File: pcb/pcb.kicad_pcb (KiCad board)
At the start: 2 copper layers, 299.5 x 113.5 mm, 228 parts, among them SW1 SW_DIP_x01_XKB_TS_2030, SW2 SW_DIP_x01_XKB_TS_2030, U1 RP2040, U2 Memory_Flash_W25Q64_XSON, U3 NCP114ASN330T1G, X1 12.000MHz

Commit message: R  pickle.py -> dumploc.py M  notes/spi M  pcb/pcb.kicad_pcb M  pcb/pcb.kicad_prl M  pcb/pcb.kicad_pro M  pcb/pcb.kicad_sch M  placefp.py M  tmr-footprints/LED-6028.kicad_mod
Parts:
- added R14: 33R, tmr-lib:R_0603_1608Metric, B.Cu at (26.9, 57.8)
- added R17: 33R, tmr-lib:R_0603_1608Metric, F.Cu at (21.4, 90.5)
- added R18: 33R, tmr-lib:R_0603_1608Metric, F.Cu at (21.4, 93.0)
- added R19: 33R, tmr-lib:R_0603_1608Metric, F.Cu at (21.4, 95.5)
- added R20: 33R, tmr-lib:R_0603_1608Metric, F.Cu at (21.4, 98.0)
- added R21: 33R, tmr-lib:R_0603_1608Metric, F.Cu at (25.4, 88.0)
- added R22: 33R, tmr-lib:R_0603_1608Metric, F.Cu at (25.4, 90.5)
- added R23: 33R, tmr-lib:R_0603_1608Metric, F.Cu at (25.4, 93.0)
- added R24: 33R, tmr-lib:R_0603_1608Metric, F.Cu at (25.4, 95.5)
- added R25: 33R, tmr-lib:R_0603_1608Metric, F.Cu at (25.4, 98.0)
- added R9: 33R, tmr-lib:R_0603_1608Metric, B.Cu at (24.9, 56.0)
- R1, R2, R3: moved to F.Cu
- moved C24 110.5 mm to (154.4, 48.0), turned to 180 degrees
- moved C22 64.6 mm to (26.6, 36.9), turned to -90 degrees
- moved ADC2 19.1 mm to (151.9, 23.9)
- moved ADC7 19.1 mm to (171.0, 23.8)
- moved C14 18.9 mm to (4.62, 49.1)
- moved ADC1 18.4 mm to (151.1, 12.4)
- moved C13 15.4 mm to (7.89, 49.2), turned to 180 degrees
- moved H4 13.3 mm to (12.3, 12.3)
- moved C19 9.56 mm to (23.2, 67.6)
- moved C9 9.04 mm to (11.2, 62.6)
- moved C23 7.58 mm to (54.9, 52.0), turned to -90 degrees
- moved C8 5.68 mm to (11.2, 64.1)
- moved C21 4.05 mm to (98.0, 34.6)
- moved C1 3.72 mm to (12.2, 51.5), turned to -90 degrees
- moved U2 3.55 mm to (17.7, 53.5)
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- renumbered LedDr1 to LD1, USBCon1 to USB1
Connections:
- ADC1 pad 10: unconnected-(ADC1-~{CS}/SHDN-Pad10) -> /GPIO2
- ADC2 pad 1: ANA_16 -> ANA_23
- ADC2 pad 10: unconnected-(ADC2-~{CS}/SHDN-Pad10) -> /GPIO3
- ADC2 pad 2: ANA_17 -> ANA_16
- ADC2 pad 3: ANA_18 -> ANA_17
- ADC2 pad 4: ANA_19 -> ANA_22
- ADC2 pad 5: ANA_20 -> ANA_21
- ADC2 pad 6: ANA_21 -> ANA_20
- ADC2 pad 7: ANA_22 -> ANA_19
- ADC2 pad 8: ANA_23 -> ANA_18
- ADC3 pad 1: ANA_30 -> ANA_31
- ADC3 pad 10: unconnected-(ADC3-~{CS}/SHDN-Pad10) -> /GPIO9
- ADC3 pad 2: ANA_31 -> ANA_32
- ADC3 pad 3: ANA_32 -> ANA_33
- ADC3 pad 4: ANA_33 -> ANA_34
- ADC3 pad 5: ANA_34 -> ANA_35
- ADC3 pad 6: ANA_35 -> ANA_36
- ADC3 pad 7: ANA_36 -> ANA_37
- ADC3 pad 8: ANA_37 -> ANA_30
- ADC4 pad 10: unconnected-(ADC4-~{CS}/SHDN-Pad10) -> /GPIO11
- ADC5 pad 10: unconnected-(ADC5-~{CS}/SHDN-Pad10) -> /GPIO12
- ADC6 pad 10: unconnected-(ADC6-~{CS}/SHDN-Pad10) -> /GPIO0
- ADC6 pad 6: ANA_14 -> ANA_29
- ADC6 pad 8: ANA_29 -> ANA_14
- ADC7 pad 1: ANA_44 -> ANA_24
- ADC7 pad 10: unconnected-(ADC7-~{CS}/SHDN-Pad10) -> /GPIO1
- ADC7 pad 2: ANA_58 -> ANA_25
- ADC7 pad 3: ANA_72 -> ANA_26
- ADC7 pad 4: ANA_24 -> ANA_27
- ADC7 pad 5: ANA_25 -> ANA_28
- ADC7 pad 6: ANA_26 -> ANA_44
- ADC7 pad 7: ANA_27 -> ANA_58
- ADC7 pad 8: ANA_28 -> ANA_72
- ADC8 pad 1: ANA_43 -> ANA_38
- ADC8 pad 10: unconnected-(ADC8-~{CS}/SHDN-Pad10) -> /GPIO14
- ADC8 pad 2: ANA_71 -> ANA_39
- ADC8 pad 3: ANA_57 -> ANA_40
- ADC8 pad 4: ANA_38 -> ANA_41
- ADC8 pad 5: ANA_39 -> ANA_42
- ADC8 pad 6: ANA_40 -> ANA_43
- ADC8 pad 7: ANA_41 -> ANA_57
- ADC8 pad 8: ANA_42 -> ANA_71
- ADC9 pad 1: ANA_69 -> ANA_56
- ADC9 pad 10: unconnected-(ADC9-~{CS}/SHDN-Pad10) -> /GPIO13
- ADC9 pad 2: ANA_68 -> ANA_70
- ADC9 pad 3: ANA_67 -> ANA_69
- ADC9 pad 4: ANA_53 -> ANA_67
- ADC9 pad 5: ANA_54 -> ANA_68
- ADC9 pad 6: ANA_55 -> ANA_53
- ADC9 pad 7: ANA_56 -> ANA_54
- ADC9 pad 8: ANA_70 -> ANA_55
- U1 pad 11: /GPIO8 -> MISO
- U1 pad 2: MISO -> /GPIO0
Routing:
- net SCK: track 0.00 -> 532.4 mm
- net MISO: track 0.00 -> 529.1 mm, vias 0 -> 2
- net MOSI: track 0.00 -> 520.4 mm, vias 0 -> 2
- net /GPIO0: track 0.00 -> 266.5 mm, vias 0 -> 4
- net /GPIO3: track 0.00 -> 265.9 mm
- net /GPIO1: track 0.00 -> 265.2 mm, vias 0 -> 4
- net /GPIO2: track 0.00 -> 259.0 mm, vias 0 -> 2
- net ANA_72: track 0.00 -> 166.6 mm
- net ANA_58: track 0.00 -> 153.8 mm
- net CA1: track 0.00 -> 147.7 mm
- net CA2: track 0.00 -> 143.3 mm
- net ANA_29: track 0.00 -> 138.5 mm
- net ANA_37: track 0.00 -> 136.5 mm
- net ANA_01: track 0.00 -> 136.4 mm
- net ANA_16: track 0.00 -> 133.8 mm
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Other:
- board text added: "${REFERENCE}"

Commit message: M  notes/spi M  pcb/pcb.kicad_pcb M  pcb/pcb.kicad_sch M  placefp.py A  tracks.py
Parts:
- removed R17, R18, R19, R20, R21, R22, R23, R24, R25: 33R, tmr-lib:R_0603_1608Metric
- moved ADC1 1.30 mm to (151.1, 13.7)
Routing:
- net GND: track 3.84 -> 651.7 mm, vias 0 -> 146
- net /GPIO14: track 0.00 -> 231.9 mm, vias 0 -> 2
- net /GPIO13: track 0.00 -> 213.3 mm, vias 0 -> 6
- net +3V3: track 2.48 -> 178.5 mm
- net /GPIO12: track 120.6 -> 137.8 mm, vias 2 -> 4
- net ANA_45: track 49.7 -> 58.1 mm
- net ANA_02: track 117.4 -> 125.4 mm
- net ANA_08: track 5.36 -> 13.2 mm
- net ANA_03: track 99.8 -> 107.6 mm
- net ANA_37: track 136.5 -> 144.3 mm
- net ANA_05: track 61.0 -> 68.6 mm
- net ANA_06: track 43.1 -> 50.7 mm
- net ANA_67: track 63.1 -> 70.7 mm
- net ANA_07: track 25.2 -> 32.8 mm
- net ANA_36: track 115.9 -> 123.4 mm
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
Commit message: M  notes/nRF52840.md A  notes/soldering M  pcb/pcb.kicad_pcb M  pcb/pcb.kicad_pro M  pcb/pcb.kicad_sch M  placefp.py M  tmr-footprints/sw_lowpro_gateron_MDT.kicad_mod M  tmr-symbols.kicad_sym M  tracks.py
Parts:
- removed C32: 100nF, tmr-lib:C_0603_1608Metric
- added F1: 500ma, Fuse:Fuse_0603_1608Metric, F.Cu at (2.87, 46.4)
- added Q2: AO3401A, Package_TO_SOT_SMD:SOT-23, B.Cu at (23.1, 73.7)
- added R17: 100k, tmr-lib:R_0603_1608Metric, B.Cu at (20.0, 73.2)
- added R18: 100R, tmr-lib:R_0603_1608Metric, B.Cu at (20.4, 68.7)
- C16: moved to B.Cu
- moved R12 253.1 mm to (12.3, 21.4), turned to -90 degrees
- moved C29 136.7 mm to (154.7, 34.3), turned to 90 degrees
- moved C31 136.1 mm to (152.6, 33.3), turned to -90 degrees
- moved C30 134.7 mm to (151.9, 35.7)
- moved R15 126.8 mm to (158.3, 35.1), turned to 90 degrees
- moved R10 123.2 mm to (156.3, 45.1), turned to 90 degrees
- moved LD1 122.1 mm to (156.8, 40.2), turned to -90 degrees
- moved R13 116.7 mm to (160.9, 34.7)
- moved R11 116.2 mm to (154.7, 45.1), turned to 90 degrees
- moved R16 114.3 mm to (157.8, 45.1), turned to -90 degrees
- moved C20 104.2 mm to (137.7, 16.2), turned to -45 degrees
- moved C26 88.2 mm to (173.3, 18.5), turned to -135 degrees
- moved C25 63.4 mm to (163.0, 10.4), turned to 0 degrees
- moved C21 57.7 mm to (153.7, 19.3), turned to 0 degrees
- moved C28 28.1 mm to (230.1, 48.7), turned to 180 degrees
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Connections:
- ADC1 pad 15: +3V3 -> VCC
- ADC1 pad 16: +3V3 -> VCC
- ADC2 pad 15: +3V3 -> VCC
- ADC2 pad 16: +3V3 -> VCC
- ADC3 pad 15: +3V3 -> VCC
- ADC3 pad 16: +3V3 -> VCC
- ADC4 pad 15: +3V3 -> VCC
- ADC4 pad 16: +3V3 -> VCC
- ADC5 pad 15: +3V3 -> VCC
- ADC5 pad 16: +3V3 -> VCC
- ADC6 pad 15: +3V3 -> VCC
- ADC6 pad 16: +3V3 -> VCC
- ADC7 pad 15: +3V3 -> VCC
- ADC7 pad 16: +3V3 -> VCC
- ADC8 pad 15: +3V3 -> VCC
- ADC8 pad 16: +3V3 -> VCC
- ADC9 pad 15: +3V3 -> VCC
- ADC9 pad 16: +3V3 -> VCC
- C20 pad 1: +3V3 -> VCC
- C21 pad 1: +3V3 -> VCC
- C22 pad 1: +3V3 -> VCC
- C23 pad 1: +3V3 -> VCC
- C24 pad 1: +3V3 -> VCC
- C25 pad 1: +3V3 -> VCC
- C26 pad 1: +3V3 -> VCC
- C27 pad 1: +3V3 -> VCC
- C28 pad 1: +3V3 -> VCC
- LD1 pad 3: /SDB -> /GPIO18
- R1 pad 2: /RESET -> /RUN
- R13 pad 2: /SDB -> /GPIO18
- S1 pad 1: +3V3 -> VCC
- S10 pad 1: +3V3 -> VCC
- S11 pad 1: +3V3 -> VCC
- S12 pad 1: +3V3 -> VCC
- S13 pad 1: +3V3 -> VCC
- S14 pad 1: +3V3 -> VCC
- S15 pad 1: +3V3 -> VCC
- S16 pad 1: +3V3 -> VCC
- S17 pad 1: +3V3 -> VCC
- S18 pad 1: +3V3 -> VCC
- S19 pad 1: +3V3 -> VCC
- S2 pad 1: +3V3 -> VCC
- S20 pad 1: +3V3 -> VCC
- S21 pad 1: +3V3 -> VCC
- S22 pad 1: +3V3 -> VCC
- S23 pad 1: +3V3 -> VCC
- S24 pad 1: +3V3 -> VCC
- S25 pad 1: +3V3 -> VCC
- S26 pad 1: +3V3 -> VCC
- S27 pad 1: +3V3 -> VCC
- S28 pad 1: +3V3 -> VCC
- S29 pad 1: +3V3 -> VCC
- S3 pad 1: +3V3 -> VCC
- S30 pad 1: +3V3 -> VCC
- S31 pad 1: +3V3 -> VCC
- S32 pad 1: +3V3 -> VCC
- S33 pad 1: +3V3 -> VCC
- S34 pad 1: +3V3 -> VCC
- S35 pad 1: +3V3 -> VCC
- S36 pad 1: +3V3 -> VCC
- S37 pad 1: +3V3 -> VCC
- S38 pad 1: +3V3 -> VCC
- S39 pad 1: +3V3 -> VCC
- S4 pad 1: +3V3 -> VCC
- S40 pad 1: +3V3 -> VCC
- S41 pad 1: +3V3 -> VCC
- S42 pad 1: +3V3 -> VCC
- S43 pad 1: +3V3 -> VCC
- S44 pad 1: +3V3 -> VCC
- S45 pad 1: +3V3 -> VCC
- S46 pad 1: +3V3 -> VCC
- S47 pad 1: +3V3 -> VCC
- S48 pad 1: +3V3 -> VCC
- S49 pad 1: +3V3 -> VCC
- S5 pad 1: +3V3 -> VCC
- S50 pad 1: +3V3 -> VCC
- S51 pad 1: +3V3 -> VCC
- S52 pad 1: +3V3 -> VCC
- S53 pad 1: +3V3 -> VCC
- S54 pad 1: +3V3 -> VCC
- S55 pad 1: +3V3 -> VCC
- S56 pad 1: +3V3 -> VCC
- S57 pad 1: +3V3 -> VCC
- S58 pad 1: +3V3 -> VCC
- S59 pad 1: +3V3 -> VCC
- S6 pad 1: +3V3 -> VCC
- S60 pad 1: +3V3 -> VCC
- S61 pad 1: +3V3 -> VCC
- S62 pad 1: +3V3 -> VCC
- S63 pad 1: +3V3 -> VCC
- S64 pad 1: +3V3 -> VCC
- S65 pad 1: +3V3 -> VCC
- S66 pad 1: +3V3 -> VCC
- S67 pad 1: +3V3 -> VCC
- S68 pad 1: +3V3 -> VCC
- S69 pad 1: +3V3 -> VCC
- S7 pad 1: +3V3 -> VCC
- S70 pad 1: +3V3 -> VCC
- S71 pad 1: +3V3 -> VCC
- S72 pad 1: +3V3 -> VCC
- S8 pad 1: +3V3 -> VCC
- S9 pad 1: +3V3 -> VCC
- SW1 pad 2: /RESET -> /RUN
- U1 pad 27: /GPIO16 -> SDA
- U1 pad 28: /GPIO17 -> SCL
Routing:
- net VCC: track 0.00 -> 2133.0 mm, vias 0 -> 89
- net CB1: track 130.4 -> 673.4 mm, vias 0 -> 10
- net CB2: track 122.8 -> 589.2 mm, vias 0 -> 13
- net CB7: track 43.7 -> 507.1 mm, vias 0 -> 15
- net CB4: track 54.7 -> 485.7 mm, vias 0 -> 24
- net CB3: track 111.0 -> 462.7 mm, vias 0 -> 18
- net GND: track 651.7 -> 304.5 mm, vias 146 -> 0
- net CB6: track 0.00 -> 340.8 mm, vias 0 -> 16
- net +5V: track 0.00 -> 261.8 mm, vias 0 -> 5
- net CA4: track 96.9 -> 333.1 mm, vias 0 -> 9
- net CB5: track 129.2 -> 307.3 mm, vias 2 -> 12
- net /RUN: track 0.00 -> 114.0 mm, vias 0 -> 3
- net CA1: track 147.7 -> 256.2 mm, vias 0 -> 7
- net CA8: track 0.00 -> 101.7 mm, vias 0 -> 7
- net CA3: track 127.6 -> 223.3 mm, vias 0 -> 8
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
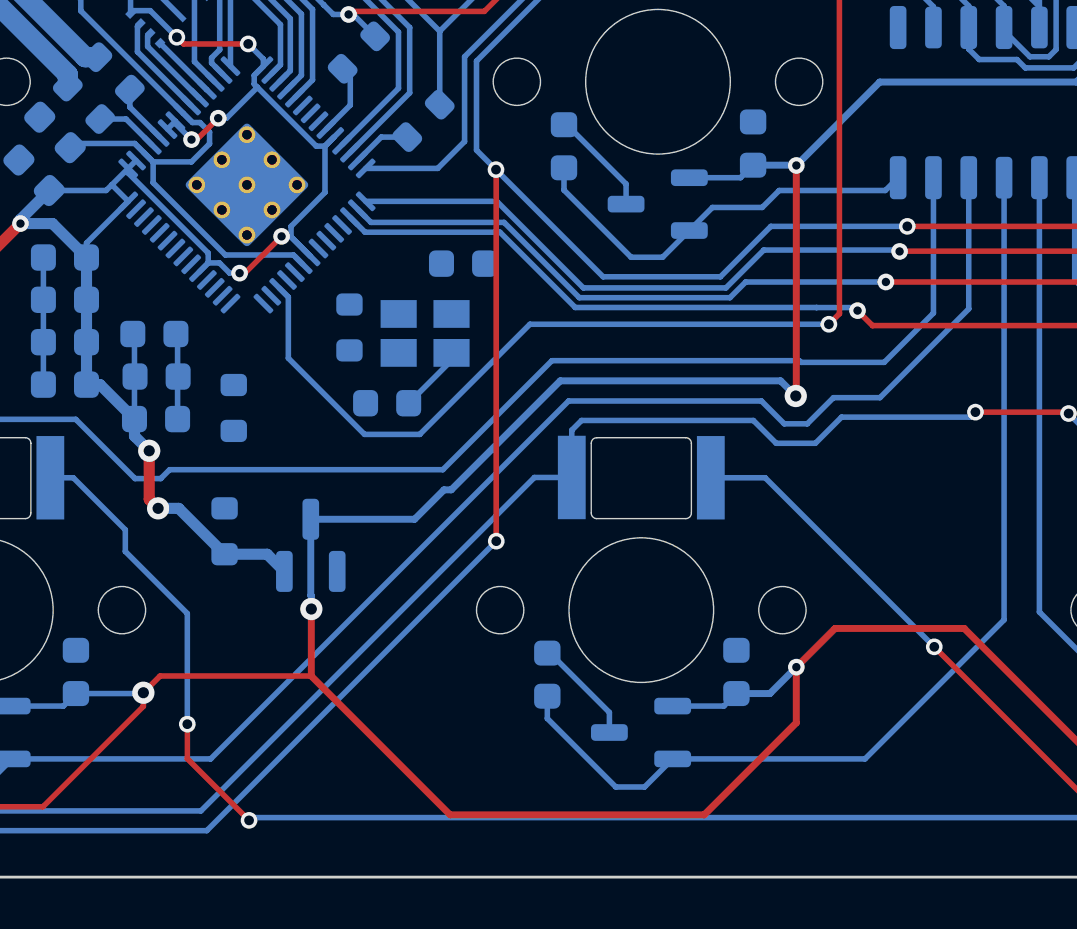
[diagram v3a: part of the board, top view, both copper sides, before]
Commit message: A  notes/analog D  notes/cnc.md D  notes/components.md R  notes/is31fl3731.md -> notes/is31fl3731 D  notes/led.md D  notes/mcu D  notes/nRF52840.md A  notes/nrf R  notes/calc.md -> notes/tmr M  pcb/pcb.kicad_pcb M  pcb/pcb.kicad_prl
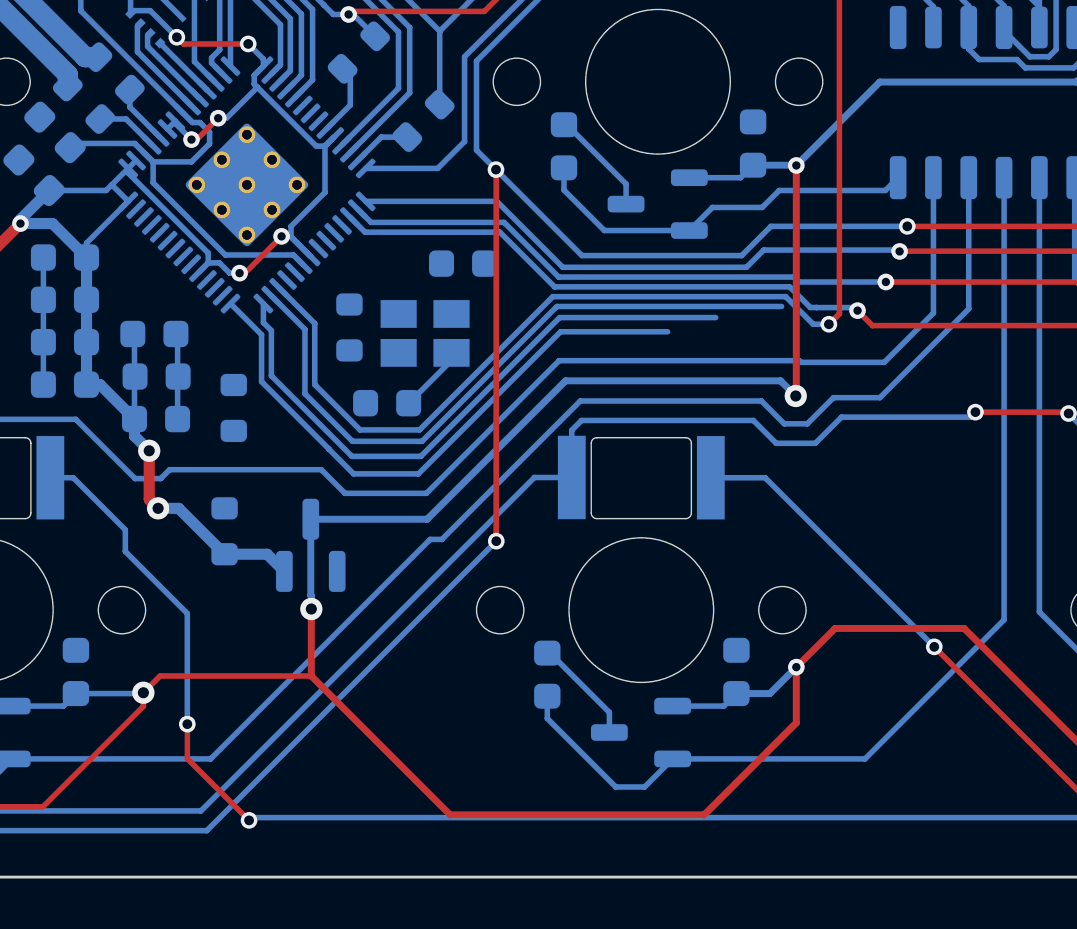
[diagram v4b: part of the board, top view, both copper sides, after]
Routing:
- net SDA: track 0.00 -> 23.9 mm
- net SCL: track 0.00 -> 22.0 mm
- net /GPIO18: track 0.00 -> 21.4 mm
- net ANA_46: track 15.0 -> 14.2 mm
- net ANA_45: track 57.8 -> 58.5 mm
- net /RUN: track 114.0 -> 114.7 mm
- net CA4: track 333.1 -> 332.4 mm
- net /GPIO12: track 137.7 -> 137.1 mm

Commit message: A  notes/bypasscaps A  notes/keytravel M  notes/leds A  notes/muxadc M  notes/notes A  notes/pulldown M  notes/scan A  notes/swupdate M  pcb/LED.kicad_sch M  pcb/pcb.kicad_pcb M  pcb/pcb.kicad_prl M  pcb/pcb.kicad_pro M  pcb/pcb.kicad_sch M  pcb/switch.kicad_sch M  placefp.py A  tmr-footprints/C_0402_1005Metric.kicad_mod M  tmr-footprints/C_0603_1608Metric.kicad_mod D  tmr-footprints/C_1206_3216Metric.kicad_mod A  tmr-footprints/Ezurio_BL54L15_Module.kicad_mod A  tmr-footprints/LED_1206_3216Metric_ReverseMount_Hole2.1mm.kicad_mod A  tmr-footprints/Murata_DFE201210U.kicad_mod A  tmr-footprints/R_0402_1005Metric.kicad_mod M  tmr-footprints/SOT-23-3.kicad_mod M  tmr-symbols.kicad_sym
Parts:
- removed ADC1, ADC2, ADC3, ADC4, ADC5, ADC6, ADC7, ADC8, ADC9: MCP3208, tmr-lib:MCP3208-SOIC-16_3.9x9.9mm_P1.27mm
- removed C12, C17: 1uF, tmr-lib:C_0603_1608Metric
- removed C13, C31: 100nF, tmr-lib:C_0603_1608Metric
- removed C14, C16: 2.2uF, tmr-lib:C_0603_1608Metric
- removed C15, C30: 10uF, tmr-lib:C_0603_1608Metric
- removed C18, C19: 15pF, tmr-lib:C_0603_1608Metric
- removed C20, C21, C22, C23, C24, C25, C26, C27, C28: C_Small_US, tmr-lib:C_0603_1608Metric
- removed C29: 10uF, tmr-lib:C_1206_3216Metric
- removed F1: 500ma, Fuse:Fuse_0603_1608Metric
- removed H2, H3, H4, H5, H6, H7, H8: MountingHole, tmr-lib:MountingHole_5.3mm_M5_ISO14580_Pad_TopBottom
- removed the Hs1 at (28.5, 8.93)
- removed LD1: IS31FL3731-QF, rp2040:QFN-28-1EP_4x4mm_P0.4mm_EP2.3x2.3mm
- removed R11, R12: 4.7k, tmr-lib:R_0603_1608Metric
- removed R13, R17: 100k, tmr-lib:R_0603_1608Metric
- removed R14: 33R, tmr-lib:R_0603_1608Metric
- removed R15, R16: 20k, tmr-lib:R_0603_1608Metric
- removed R18: 100R, tmr-lib:R_0603_1608Metric
- removed SW2: SW_DIP_x01_XKB_TS_2030, Button_Switch_SMD:SW_SPST_B3U-3000P
- removed USB1: USB_TYPE_C_Receptacle_16P, Connector_USB:USB_C_Receptacle_G-Switch_GT-USB-7025
- removed X1: 12.000MHz, rp2040:Crystal_SMD_2520-4Pin_2.5x2.0mm-Handsolder
- added BAT1: Battery_Pack_PS5, Connector_JST:JST_EH_S3B-EH_1x03_P2.50mm_Horizontal, F.Cu at (-5.04, 80.6)
- added Cvcc1: 0.1uF, tmr-lib:C_0402_1005Metric, B.Cu at (16.0, 4.00)
- added Cvcc10: 0.1uF, tmr-lib:C_0402_1005Metric, B.Cu at (187.0, 4.00)
- added Cvcc11: 0.1uF, tmr-lib:C_0402_1005Metric, B.Cu at (206.0, 4.00)
- added Cvcc12: 0.1uF, tmr-lib:C_0402_1005Metric, B.Cu at (225.0, 4.00)
- added Cvcc13: 0.1uF, tmr-lib:C_0402_1005Metric, B.Cu at (244.0, 4.00)
- added Cvcc14: 0.1uF, tmr-lib:C_0402_1005Metric, B.Cu at (263.0, 4.00)
- added Cvcc15: 0.1uF, tmr-lib:C_0402_1005Metric, B.Cu at (282.0, 4.00)
- added Cvcc16: 0.1uF, tmr-lib:C_0402_1005Metric, B.Cu at (20.8, 23.0)
- added Cvcc17: 0.1uF, tmr-lib:C_0402_1005Metric, B.Cu at (44.5, 23.0)
- added Cvcc18: 0.1uF, tmr-lib:C_0402_1005Metric, B.Cu at (63.5, 23.0)
- added Cvcc19: 0.1uF, tmr-lib:C_0402_1005Metric, B.Cu at (82.5, 23.0)
- added Cvcc2: 0.1uF, tmr-lib:C_0402_1005Metric, B.Cu at (35.0, 4.00)
- added Cvcc20: 0.1uF, tmr-lib:C_0402_1005Metric, B.Cu at (101.5, 23.0)
- added Cvcc21: 0.1uF, tmr-lib:C_0402_1005Metric, B.Cu at (120.5, 23.0)
- added Cvcc22: 0.1uF, tmr-lib:C_0402_1005Metric, B.Cu at (139.5, 23.0)
- added Cvcc23: 0.1uF, tmr-lib:C_0402_1005Metric, B.Cu at (158.5, 23.0)
- added Cvcc24: 0.1uF, tmr-lib:C_0402_1005Metric, B.Cu at (177.5, 23.0)
- added Cvcc25: 0.1uF, tmr-lib:C_0402_1005Metric, B.Cu at (196.5, 23.0)
- added Cvcc26: 0.1uF, tmr-lib:C_0402_1005Metric, B.Cu at (215.5, 23.0)
- added Cvcc27: 0.1uF, tmr-lib:C_0402_1005Metric, B.Cu at (234.5, 23.0)
- added Cvcc28: 0.1uF, tmr-lib:C_0402_1005Metric, B.Cu at (253.5, 23.0)
- added Cvcc29: 0.1uF, tmr-lib:C_0402_1005Metric, B.Cu at (277.2, 23.0)
- added Cvcc3: 0.1uF, tmr-lib:C_0402_1005Metric, B.Cu at (54.0, 4.00)
- added Cvcc30: 0.1uF, tmr-lib:C_0402_1005Metric, B.Cu at (8.88, 42.0)
- added Cvcc31: 0.1uF, tmr-lib:C_0402_1005Metric, B.Cu at (30.2, 42.0)
- added Cvcc32: 0.1uF, tmr-lib:C_0402_1005Metric, B.Cu at (49.2, 42.0)
- added Cvcc33: 0.1uF, tmr-lib:C_0402_1005Metric, B.Cu at (68.2, 42.0)
- added Cvcc34: 0.1uF, tmr-lib:C_0402_1005Metric, B.Cu at (87.2, 42.0)
- added Cvcc35: 0.1uF, tmr-lib:C_0402_1005Metric, B.Cu at (106.2, 42.0)
- added Cvcc36: 0.1uF, tmr-lib:C_0402_1005Metric, B.Cu at (125.2, 42.0)
- added Cvcc37: 0.1uF, tmr-lib:C_0402_1005Metric, B.Cu at (144.2, 42.0)
- added Cvcc38: 0.1uF, tmr-lib:C_0402_1005Metric, B.Cu at (163.2, 42.0)
- added Cvcc39: 0.1uF, tmr-lib:C_0402_1005Metric, B.Cu at (182.2, 42.0)
- added Cvcc4: 0.1uF, tmr-lib:C_0402_1005Metric, B.Cu at (73.0, 4.00)
- added Cvcc40: 0.1uF, tmr-lib:C_0402_1005Metric, B.Cu at (201.2, 42.0)
- added Cvcc41: 0.1uF, tmr-lib:C_0402_1005Metric, B.Cu at (220.2, 42.0)
- added Cvcc42: 0.1uF, tmr-lib:C_0402_1005Metric, B.Cu at (241.6, 42.0)
- added Cvcc43: 0.1uF, tmr-lib:C_0402_1005Metric, B.Cu at (263.0, 42.0)
- added Cvcc44: 0.1uF, tmr-lib:C_0402_1005Metric, B.Cu at (282.0, 42.0)
- added Cvcc45: 0.1uF, tmr-lib:C_0402_1005Metric, B.Cu at (4.12, 61.0)
- added Cvcc46: 0.1uF, tmr-lib:C_0402_1005Metric, B.Cu at (32.6, 61.0)
- added Cvcc47: 0.1uF, tmr-lib:C_0402_1005Metric, B.Cu at (58.8, 61.0)
- added Cvcc48: 0.1uF, tmr-lib:C_0402_1005Metric, B.Cu at (77.8, 61.0)
- added Cvcc49: 0.1uF, tmr-lib:C_0402_1005Metric, B.Cu at (96.8, 61.0)
- added Cvcc5: 0.1uF, tmr-lib:C_0402_1005Metric, B.Cu at (92.0, 4.00)
- added Cvcc50: 0.1uF, tmr-lib:C_0402_1005Metric, B.Cu at (115.8, 61.0)
- added Cvcc51: 0.1uF, tmr-lib:C_0402_1005Metric, B.Cu at (134.8, 61.0)
- added Cvcc52: 0.1uF, tmr-lib:C_0402_1005Metric, B.Cu at (153.8, 61.0)
- added Cvcc53: 0.1uF, tmr-lib:C_0402_1005Metric, B.Cu at (172.8, 61.0)
- added Cvcc54: 0.1uF, tmr-lib:C_0402_1005Metric, B.Cu at (191.8, 61.0)
- added Cvcc55: 0.1uF, tmr-lib:C_0402_1005Metric, B.Cu at (210.8, 61.0)
- added Cvcc56: 0.1uF, tmr-lib:C_0402_1005Metric, B.Cu at (229.8, 61.0)
- added Cvcc57: 0.1uF, tmr-lib:C_0402_1005Metric, B.Cu at (255.9, 61.0)
- added Cvcc58: 0.1uF, tmr-lib:C_0402_1005Metric, B.Cu at (282.0, 61.0)
- added Cvcc59: 0.1uF, tmr-lib:C_0402_1005Metric, B.Cu at (8.28, 80.0)
- added Cvcc6: 0.1uF, tmr-lib:C_0402_1005Metric, B.Cu at (111.0, 4.00)
- added Cvcc60: 0.1uF, tmr-lib:C_0402_1005Metric, B.Cu at (32.0, 80.0)
- added Cvcc61: 0.1uF, tmr-lib:C_0402_1005Metric, B.Cu at (53.4, 80.0)
- added Cvcc62: 0.1uF, tmr-lib:C_0402_1005Metric, B.Cu at (73.4, 82.2)
- added Cvcc63: 0.1uF, tmr-lib:C_0402_1005Metric, B.Cu at (91.4, 88.7)
- added Cvcc64: 0.1uF, tmr-lib:C_0402_1005Metric, B.Cu at (109.2, 95.2)
- added Cvcc65: 0.1uF, tmr-lib:C_0402_1005Metric, B.Cu at (134.8, 80.0)
- added Cvcc66: 0.1uF, tmr-lib:C_0402_1005Metric, B.Cu at (160.6, 97.3)
- added Cvcc67: 0.1uF, tmr-lib:C_0402_1005Metric, B.Cu at (178.4, 90.8)
- added Cvcc68: 0.1uF, tmr-lib:C_0402_1005Metric, B.Cu at (196.3, 84.3)
- added Cvcc69: 0.1uF, tmr-lib:C_0402_1005Metric, B.Cu at (216.1, 80.0)
- added Cvcc7: 0.1uF, tmr-lib:C_0402_1005Metric, B.Cu at (130.0, 4.00)
- added Cvcc70: 0.1uF, tmr-lib:C_0402_1005Metric, B.Cu at (237.5, 80.0)
- added Cvcc71: 0.1uF, tmr-lib:C_0402_1005Metric, B.Cu at (258.9, 80.0)
- added Cvcc72: 0.1uF, tmr-lib:C_0402_1005Metric, B.Cu at (277.9, 80.0)
- added Cvcc8: 0.1uF, tmr-lib:C_0402_1005Metric, B.Cu at (149.0, 4.00)
- added Cvcc9: 0.1uF, tmr-lib:C_0402_1005Metric, B.Cu at (168.0, 4.00)
- added Cvout1: 0.1nF, tmr-lib:C_0402_1005Metric, B.Cu at (16.0, 2.00)
- added Cvout10: 0.1nF, tmr-lib:C_0402_1005Metric, B.Cu at (187.0, 2.00)
- added Cvout11: 0.1nF, tmr-lib:C_0402_1005Metric, B.Cu at (206.0, 2.00)
- added Cvout12: 0.1nF, tmr-lib:C_0402_1005Metric, B.Cu at (225.0, 2.00)
- added Cvout13: 0.1nF, tmr-lib:C_0402_1005Metric, B.Cu at (244.0, 2.00)
- added Cvout14: 0.1nF, tmr-lib:C_0402_1005Metric, B.Cu at (263.0, 2.00)
- added Cvout15: 0.1nF, tmr-lib:C_0402_1005Metric, B.Cu at (282.0, 2.00)
- added Cvout16: 0.1nF, tmr-lib:C_0402_1005Metric, B.Cu at (20.8, 21.0)
- added Cvout17: 0.1nF, tmr-lib:C_0402_1005Metric, B.Cu at (44.5, 21.0)
- added Cvout18: 0.1nF, tmr-lib:C_0402_1005Metric, B.Cu at (63.5, 21.0)
- added Cvout19: 0.1nF, tmr-lib:C_0402_1005Metric, B.Cu at (82.5, 21.0)
- added Cvout2: 0.1nF, tmr-lib:C_0402_1005Metric, B.Cu at (35.0, 2.00)
- added Cvout20: 0.1nF, tmr-lib:C_0402_1005Metric, B.Cu at (101.5, 21.0)
- added Cvout21: 0.1nF, tmr-lib:C_0402_1005Metric, B.Cu at (120.5, 21.0)
- added Cvout22: 0.1nF, tmr-lib:C_0402_1005Metric, B.Cu at (139.5, 21.0)
- added Cvout23: 0.1nF, tmr-lib:C_0402_1005Metric, B.Cu at (158.5, 21.0)
- added Cvout24: 0.1nF, tmr-lib:C_0402_1005Metric, B.Cu at (177.5, 21.0)
- added Cvout25: 0.1nF, tmr-lib:C_0402_1005Metric, B.Cu at (196.5, 21.0)
- added Cvout26: 0.1nF, tmr-lib:C_0402_1005Metric, B.Cu at (215.5, 21.0)
- added Cvout27: 0.1nF, tmr-lib:C_0402_1005Metric, B.Cu at (234.5, 21.0)
- added Cvout28: 0.1nF, tmr-lib:C_0402_1005Metric, B.Cu at (253.5, 21.0)
- added Cvout29: 0.1nF, tmr-lib:C_0402_1005Metric, B.Cu at (277.2, 21.0)
- added Cvout3: 0.1nF, tmr-lib:C_0402_1005Metric, B.Cu at (54.0, 2.00)
- added Cvout30: 0.1nF, tmr-lib:C_0402_1005Metric, B.Cu at (8.88, 40.0)
- added Cvout31: 0.1nF, tmr-lib:C_0402_1005Metric, B.Cu at (30.2, 40.0)
- added Cvout32: 0.1nF, tmr-lib:C_0402_1005Metric, B.Cu at (49.2, 40.0)
- added Cvout33: 0.1nF, tmr-lib:C_0402_1005Metric, B.Cu at (68.2, 40.0)
- added Cvout34: 0.1nF, tmr-lib:C_0402_1005Metric, B.Cu at (87.2, 40.0)
- added Cvout35: 0.1nF, tmr-lib:C_0402_1005Metric, B.Cu at (106.2, 40.0)
- added Cvout36: 0.1nF, tmr-lib:C_0402_1005Metric, B.Cu at (125.2, 40.0)
- added Cvout37: 0.1nF, tmr-lib:C_0402_1005Metric, B.Cu at (144.2, 40.0)
- added Cvout38: 0.1nF, tmr-lib:C_0402_1005Metric, B.Cu at (163.2, 40.0)
- added Cvout39: 0.1nF, tmr-lib:C_0402_1005Metric, B.Cu at (182.2, 40.0)
- added Cvout4: 0.1nF, tmr-lib:C_0402_1005Metric, B.Cu at (73.0, 2.00)
- added Cvout40: 0.1nF, tmr-lib:C_0402_1005Metric, B.Cu at (201.2, 40.0)
- added Cvout41: 0.1nF, tmr-lib:C_0402_1005Metric, B.Cu at (220.2, 40.0)
- added Cvout42: 0.1nF, tmr-lib:C_0402_1005Metric, B.Cu at (241.6, 40.0)
- added Cvout43: 0.1nF, tmr-lib:C_0402_1005Metric, B.Cu at (263.0, 40.0)
- added Cvout44: 0.1nF, tmr-lib:C_0402_1005Metric, B.Cu at (282.0, 40.0)
- added Cvout45: 0.1nF, tmr-lib:C_0402_1005Metric, B.Cu at (4.12, 59.0)
- added Cvout46: 0.1nF, tmr-lib:C_0402_1005Metric, B.Cu at (32.6, 59.0)
- added Cvout47: 0.1nF, tmr-lib:C_0402_1005Metric, B.Cu at (58.8, 59.0)
- added Cvout48: 0.1nF, tmr-lib:C_0402_1005Metric, B.Cu at (77.8, 59.0)
- added Cvout49: 0.1nF, tmr-lib:C_0402_1005Metric, B.Cu at (96.8, 59.0)
- added Cvout5: 0.1nF, tmr-lib:C_0402_1005Metric, B.Cu at (92.0, 2.00)
- added Cvout50: 0.1nF, tmr-lib:C_0402_1005Metric, B.Cu at (115.8, 59.0)
- added Cvout51: 0.1nF, tmr-lib:C_0402_1005Metric, B.Cu at (134.8, 59.0)
- added Cvout52: 0.1nF, tmr-lib:C_0402_1005Metric, B.Cu at (153.8, 59.0)
- added Cvout53: 0.1nF, tmr-lib:C_0402_1005Metric, B.Cu at (172.8, 59.0)
- added Cvout54: 0.1nF, tmr-lib:C_0402_1005Metric, B.Cu at (191.8, 59.0)
- added Cvout55: 0.1nF, tmr-lib:C_0402_1005Metric, B.Cu at (210.8, 59.0)
- added Cvout56: 0.1nF, tmr-lib:C_0402_1005Metric, B.Cu at (229.8, 59.0)
- added Cvout57: 0.1nF, tmr-lib:C_0402_1005Metric, B.Cu at (255.9, 59.0)
- added Cvout58: 0.1nF, tmr-lib:C_0402_1005Metric, B.Cu at (282.0, 59.0)
- added Cvout59: 0.1nF, tmr-lib:C_0402_1005Metric, B.Cu at (8.28, 78.0)
- added Cvout6: 0.1nF, tmr-lib:C_0402_1005Metric, B.Cu at (111.0, 2.00)
- added Cvout60: 0.1nF, tmr-lib:C_0402_1005Metric, B.Cu at (32.0, 78.0)
- added Cvout61: 0.1nF, tmr-lib:C_0402_1005Metric, B.Cu at (53.4, 78.0)
- added Cvout62: 0.1nF, tmr-lib:C_0402_1005Metric, B.Cu at (74.1, 80.4)
- added Cvout63: 0.1nF, tmr-lib:C_0402_1005Metric, B.Cu at (92.1, 86.9)
- added Cvout64: 0.1nF, tmr-lib:C_0402_1005Metric, B.Cu at (109.9, 93.4)
- added Cvout65: 0.1nF, tmr-lib:C_0402_1005Metric, B.Cu at (134.8, 78.0)
- added Cvout66: 0.1nF, tmr-lib:C_0402_1005Metric, B.Cu at (160.0, 95.4)
- added Cvout67: 0.1nF, tmr-lib:C_0402_1005Metric, B.Cu at (177.8, 88.9)
- added Cvout68: 0.1nF, tmr-lib:C_0402_1005Metric, B.Cu at (195.6, 82.4)
- added Cvout69: 0.1nF, tmr-lib:C_0402_1005Metric, B.Cu at (216.1, 78.0)
- added Cvout7: 0.1nF, tmr-lib:C_0402_1005Metric, B.Cu at (130.0, 2.00)
- added Cvout70: 0.1nF, tmr-lib:C_0402_1005Metric, B.Cu at (237.5, 78.0)
- added Cvout71: 0.1nF, tmr-lib:C_0402_1005Metric, B.Cu at (258.9, 78.0)
- added Cvout72: 0.1nF, tmr-lib:C_0402_1005Metric, B.Cu at (277.9, 78.0)
- added Cvout8: 0.1nF, tmr-lib:C_0402_1005Metric, B.Cu at (149.0, 2.00)
- added Cvout9: 0.1nF, tmr-lib:C_0402_1005Metric, B.Cu at (168.0, 2.00)
- added Hs11: M2_Pad, MountingHole:MountingHole_2.2mm_M2_ISO7380_Pad_TopBottom, F.Cu at (275.5, 65.9)
- added Hs12: M2_Pad, MountingHole:MountingHole_2.2mm_M2_ISO7380_Pad_TopBottom, F.Cu at (-48.9, 53.2)
- added L1: 2.2uF, tmr-lib:Murata_DFE201210U, F.Cu at (-25.5, 72.8)
- added M1: nRF54L15 module, tmr-lib:Ezurio_BL54L15_Module, B.Cu at (27.4, 71.5)
- added Q1: DMC2400UV, Package_TO_SOT_SMD:SOT-563, B.Cu at (1.48, 67.8)
- added Rd1: 220R, tmr-lib:R_0402_1005Metric, B.Cu at (22.1, -4.75)
- added Rd10: 220R, tmr-lib:R_0402_1005Metric, B.Cu at (193.1, -4.75)
- added Rd11: 220R, tmr-lib:R_0402_1005Metric, B.Cu at (212.1, -4.75)
- added Rd12: 220R, tmr-lib:R_0402_1005Metric, B.Cu at (231.1, -4.75)
- added Rd13: 220R, tmr-lib:R_0402_1005Metric, B.Cu at (250.1, -4.75)
- added Rd14: 220R, tmr-lib:R_0402_1005Metric, B.Cu at (269.1, -4.75)
- added Rd15: 220R, tmr-lib:R_0402_1005Metric, B.Cu at (288.1, -4.75)
- added Rd16: 220R, tmr-lib:R_0402_1005Metric, B.Cu at (26.9, 14.2)
- added Rd17: 220R, tmr-lib:R_0402_1005Metric, B.Cu at (50.6, 14.2)
- added Rd18: 220R, tmr-lib:R_0402_1005Metric, B.Cu at (69.6, 14.2)
- added Rd19: 220R, tmr-lib:R_0402_1005Metric, B.Cu at (88.6, 14.2)
- added Rd2: 220R, tmr-lib:R_0402_1005Metric, B.Cu at (41.1, -4.75)
- added Rd20: 220R, tmr-lib:R_0402_1005Metric, B.Cu at (107.6, 14.2)
- added Rd21: 220R, tmr-lib:R_0402_1005Metric, B.Cu at (126.6, 14.2)
- added Rd22: 220R, tmr-lib:R_0402_1005Metric, B.Cu at (145.6, 14.2)
- added Rd23: 220R, tmr-lib:R_0402_1005Metric, B.Cu at (164.6, 14.2)
- added Rd24: 220R, tmr-lib:R_0402_1005Metric, B.Cu at (183.6, 14.2)
- added Rd25: 220R, tmr-lib:R_0402_1005Metric, B.Cu at (202.6, 14.2)
- added Rd26: 220R, tmr-lib:R_0402_1005Metric, B.Cu at (221.6, 14.2)
- added Rd27: 220R, tmr-lib:R_0402_1005Metric, B.Cu at (240.6, 14.2)
- added Rd28: 220R, tmr-lib:R_0402_1005Metric, B.Cu at (259.6, 14.2)
- added Rd29: 220R, tmr-lib:R_0402_1005Metric, B.Cu at (283.4, 14.2)
- added Rd3: 220R, tmr-lib:R_0402_1005Metric, B.Cu at (60.1, -4.75)
- added Rd30: 220R, tmr-lib:R_0402_1005Metric, B.Cu at (15.0, 33.2)
- added Rd31: 220R, tmr-lib:R_0402_1005Metric, B.Cu at (36.4, 33.2)
- added Rd32: 220R, tmr-lib:R_0402_1005Metric, B.Cu at (55.4, 33.2)
- added Rd33: 220R, tmr-lib:R_0402_1005Metric, B.Cu at (74.3, 33.2)
- added Rd34: 220R, tmr-lib:R_0402_1005Metric, B.Cu at (93.3, 33.2)
- added Rd35: 220R, tmr-lib:R_0402_1005Metric, B.Cu at (112.3, 33.2)
- added Rd36: 220R, tmr-lib:R_0402_1005Metric, B.Cu at (131.3, 33.2)
- added Rd37: 220R, tmr-lib:R_0402_1005Metric, B.Cu at (150.3, 33.2)
- added Rd38: 220R, tmr-lib:R_0402_1005Metric, B.Cu at (169.3, 33.2)
- added Rd39: 220R, tmr-lib:R_0402_1005Metric, B.Cu at (188.3, 33.2)
- added Rd4: 220R, tmr-lib:R_0402_1005Metric, B.Cu at (79.1, -4.75)
- added Rd40: 220R, tmr-lib:R_0402_1005Metric, B.Cu at (207.3, 33.2)
- added Rd41: 220R, tmr-lib:R_0402_1005Metric, B.Cu at (226.3, 33.2)
- added Rd42: 220R, tmr-lib:R_0402_1005Metric, B.Cu at (247.7, 33.2)
- added Rd43: 220R, tmr-lib:R_0402_1005Metric, B.Cu at (269.1, 33.2)
- added Rd44: 220R, tmr-lib:R_0402_1005Metric, B.Cu at (288.1, 33.2)
- added Rd45: 220R, tmr-lib:R_0402_1005Metric, B.Cu at (10.2, 52.2)
- added Rd46: 220R, tmr-lib:R_0402_1005Metric, B.Cu at (38.7, 52.2)
- added Rd47: 220R, tmr-lib:R_0402_1005Metric, B.Cu at (64.8, 52.2)
- added Rd48: 220R, tmr-lib:R_0402_1005Metric, B.Cu at (83.8, 52.2)
- added Rd49: 220R, tmr-lib:R_0402_1005Metric, B.Cu at (102.8, 52.2)
- added Rd5: 220R, tmr-lib:R_0402_1005Metric, B.Cu at (98.1, -4.75)
- added Rd50: 220R, tmr-lib:R_0402_1005Metric, B.Cu at (121.8, 52.2)
- added Rd51: 220R, tmr-lib:R_0402_1005Metric, B.Cu at (140.8, 52.2)
- added Rd52: 220R, tmr-lib:R_0402_1005Metric, B.Cu at (159.8, 52.2)
- added Rd53: 220R, tmr-lib:R_0402_1005Metric, B.Cu at (178.8, 52.2)
- added Rd54: 220R, tmr-lib:R_0402_1005Metric, B.Cu at (197.8, 52.2)
- added Rd55: 220R, tmr-lib:R_0402_1005Metric, B.Cu at (216.8, 52.2)
- added Rd56: 220R, tmr-lib:R_0402_1005Metric, B.Cu at (235.8, 52.2)
- added Rd57: 220R, tmr-lib:R_0402_1005Metric, B.Cu at (262.0, 52.2)
- added Rd58: 220R, tmr-lib:R_0402_1005Metric, B.Cu at (288.1, 52.2)
- added Rd59: 220R, tmr-lib:R_0402_1005Metric, B.Cu at (14.4, 71.2)
- added Rd6: 220R, tmr-lib:R_0402_1005Metric, B.Cu at (117.1, -4.75)
- added Rd60: 220R, tmr-lib:R_0402_1005Metric, B.Cu at (38.1, 71.2)
- added Rd61: 220R, tmr-lib:R_0402_1005Metric, B.Cu at (59.5, 71.2)
- added Rd62: 220R, tmr-lib:R_0402_1005Metric, B.Cu at (82.2, 76.1)
- added Rd63: 220R, tmr-lib:R_0402_1005Metric, B.Cu at (100.1, 82.6)
- added Rd64: 220R, tmr-lib:R_0402_1005Metric, B.Cu at (117.9, 89.1)
- added Rd65: 220R, tmr-lib:R_0402_1005Metric, B.Cu at (140.8, 71.2)
- added Rd66: 220R, tmr-lib:R_0402_1005Metric, B.Cu at (163.4, 87.0)
- added Rd67: 220R, tmr-lib:R_0402_1005Metric, B.Cu at (181.2, 80.5)
- added Rd68: 220R, tmr-lib:R_0402_1005Metric, B.Cu at (199.0, 74.0)
- added Rd69: 220R, tmr-lib:R_0402_1005Metric, B.Cu at (222.2, 71.2)
- added Rd7: 220R, tmr-lib:R_0402_1005Metric, B.Cu at (136.1, -4.75)
- added Rd70: 220R, tmr-lib:R_0402_1005Metric, B.Cu at (243.6, 71.2)
- added Rd71: 220R, tmr-lib:R_0402_1005Metric, B.Cu at (264.9, 71.2)
- added Rd72: 220R, tmr-lib:R_0402_1005Metric, B.Cu at (283.9, 71.2)
- added Rd8: 220R, tmr-lib:R_0402_1005Metric, B.Cu at (155.1, -4.75)
- added Rd9: 220R, tmr-lib:R_0402_1005Metric, B.Cu at (174.1, -4.75)
- added TMR1: TMR2617, tmr-lib:SOT-23-3, B.Cu at (19.0, 4.40)
- added TMR10: TMR2617, tmr-lib:SOT-23-3, B.Cu at (190.0, 4.40)
- added TMR11: TMR2617, tmr-lib:SOT-23-3, B.Cu at (209.0, 4.40)
- added TMR12: TMR2617, tmr-lib:SOT-23-3, B.Cu at (228.0, 4.40)
- added TMR13: TMR2617, tmr-lib:SOT-23-3, B.Cu at (247.0, 4.40)
- added TMR14: TMR2617, tmr-lib:SOT-23-3, B.Cu at (266.0, 4.40)
- added TMR15: TMR2617, tmr-lib:SOT-23-3, B.Cu at (285.0, 4.40)
- added TMR16: TMR2617, tmr-lib:SOT-23-3, B.Cu at (23.8, 23.4)
- added TMR17: TMR2617, tmr-lib:SOT-23-3, B.Cu at (47.5, 23.4)
- added TMR18: TMR2617, tmr-lib:SOT-23-3, B.Cu at (66.5, 23.4)
- added TMR19: TMR2617, tmr-lib:SOT-23-3, B.Cu at (85.5, 23.4)
- added TMR2: TMR2617, tmr-lib:SOT-23-3, B.Cu at (38.0, 4.40)
- added TMR20: TMR2617, tmr-lib:SOT-23-3, B.Cu at (104.5, 23.4)
- added TMR21: TMR2617, tmr-lib:SOT-23-3, B.Cu at (123.5, 23.4)
- added TMR22: TMR2617, tmr-lib:SOT-23-3, B.Cu at (142.5, 23.4)
- added TMR23: TMR2617, tmr-lib:SOT-23-3, B.Cu at (161.5, 23.4)
- added TMR24: TMR2617, tmr-lib:SOT-23-3, B.Cu at (180.5, 23.4)
- added TMR25: TMR2617, tmr-lib:SOT-23-3, B.Cu at (199.5, 23.4)
- added TMR26: TMR2617, tmr-lib:SOT-23-3, B.Cu at (218.5, 23.4)
- added TMR27: TMR2617, tmr-lib:SOT-23-3, B.Cu at (237.5, 23.4)
- added TMR28: TMR2617, tmr-lib:SOT-23-3, B.Cu at (256.5, 23.4)
- added TMR29: TMR2617, tmr-lib:SOT-23-3, B.Cu at (280.2, 23.4)
- added TMR3: TMR2617, tmr-lib:SOT-23-3, B.Cu at (57.0, 4.40)
- added TMR30: TMR2617, tmr-lib:SOT-23-3, B.Cu at (11.9, 42.4)
- added TMR31: TMR2617, tmr-lib:SOT-23-3, B.Cu at (33.2, 42.4)
- added TMR32: TMR2617, tmr-lib:SOT-23-3, B.Cu at (52.2, 42.4)
- added TMR33: TMR2617, tmr-lib:SOT-23-3, B.Cu at (71.2, 42.4)
- added TMR34: TMR2617, tmr-lib:SOT-23-3, B.Cu at (90.2, 42.4)
- added TMR35: TMR2617, tmr-lib:SOT-23-3, B.Cu at (109.2, 42.4)
- added TMR36: TMR2617, tmr-lib:SOT-23-3, B.Cu at (128.2, 42.4)
- added TMR37: TMR2617, tmr-lib:SOT-23-3, B.Cu at (147.2, 42.4)
- added TMR38: TMR2617, tmr-lib:SOT-23-3, B.Cu at (166.2, 42.4)
- added TMR39: TMR2617, tmr-lib:SOT-23-3, B.Cu at (185.2, 42.4)
- added TMR4: TMR2617, tmr-lib:SOT-23-3, B.Cu at (76.0, 4.40)
- added TMR40: TMR2617, tmr-lib:SOT-23-3, B.Cu at (204.2, 42.4)
- added TMR41: TMR2617, tmr-lib:SOT-23-3, B.Cu at (223.2, 42.4)
- added TMR42: TMR2617, tmr-lib:SOT-23-3, B.Cu at (244.6, 42.4)
- added TMR43: TMR2617, tmr-lib:SOT-23-3, B.Cu at (266.0, 42.4)
- added TMR44: TMR2617, tmr-lib:SOT-23-3, B.Cu at (285.0, 42.4)
- added TMR45: TMR2617, tmr-lib:SOT-23-3, B.Cu at (7.12, 61.4)
- added TMR46: TMR2617, tmr-lib:SOT-23-3, B.Cu at (35.6, 61.4)
- added TMR47: TMR2617, tmr-lib:SOT-23-3, B.Cu at (61.8, 61.4)
- added TMR48: TMR2617, tmr-lib:SOT-23-3, B.Cu at (80.8, 61.4)
- added TMR49: TMR2617, tmr-lib:SOT-23-3, B.Cu at (99.8, 61.4)
- added TMR5: TMR2617, tmr-lib:SOT-23-3, B.Cu at (95.0, 4.40)
- added TMR50: TMR2617, tmr-lib:SOT-23-3, B.Cu at (118.8, 61.4)
- added TMR51: TMR2617, tmr-lib:SOT-23-3, B.Cu at (137.8, 61.4)
- added TMR52: TMR2617, tmr-lib:SOT-23-3, B.Cu at (156.8, 61.4)
- added TMR53: TMR2617, tmr-lib:SOT-23-3, B.Cu at (175.8, 61.4)
- added TMR54: TMR2617, tmr-lib:SOT-23-3, B.Cu at (194.8, 61.4)
- added TMR55: TMR2617, tmr-lib:SOT-23-3, B.Cu at (213.8, 61.4)
- added TMR56: TMR2617, tmr-lib:SOT-23-3, B.Cu at (232.8, 61.4)
- added TMR57: TMR2617, tmr-lib:SOT-23-3, B.Cu at (258.9, 61.4)
- added TMR58: TMR2617, tmr-lib:SOT-23-3, B.Cu at (285.0, 61.4)
- added TMR59: TMR2617, tmr-lib:SOT-23-3, B.Cu at (11.3, 80.4)
- added TMR6: TMR2617, tmr-lib:SOT-23-3, B.Cu at (114.0, 4.40)
- added TMR60: TMR2617, tmr-lib:SOT-23-3, B.Cu at (35.0, 80.4)
- added TMR61: TMR2617, tmr-lib:SOT-23-3, B.Cu at (56.4, 80.4)
- added TMR62: TMR2617, tmr-lib:SOT-23-3, B.Cu at (76.1, 83.6)
- added TMR63: TMR2617, tmr-lib:SOT-23-3, B.Cu at (94.1, 90.1)
- added TMR64: TMR2617, tmr-lib:SOT-23-3, B.Cu at (111.9, 96.6)
- added TMR65: TMR2617, tmr-lib:SOT-23-3, B.Cu at (137.8, 80.4)
- added TMR66: TMR2617, tmr-lib:SOT-23-3, B.Cu at (163.6, 96.6)
- added TMR67: TMR2617, tmr-lib:SOT-23-3, B.Cu at (181.4, 90.1)
- added TMR68: TMR2617, tmr-lib:SOT-23-3, B.Cu at (199.3, 83.6)
- added TMR69: TMR2617, tmr-lib:SOT-23-3, B.Cu at (219.1, 80.4)
- added TMR7: TMR2617, tmr-lib:SOT-23-3, B.Cu at (133.0, 4.40)
- added TMR70: TMR2617, tmr-lib:SOT-23-3, B.Cu at (240.5, 80.4)
- added TMR71: TMR2617, tmr-lib:SOT-23-3, B.Cu at (261.9, 80.4)
- added TMR72: TMR2617, tmr-lib:SOT-23-3, B.Cu at (280.9, 80.4)
- added TMR8: TMR2617, tmr-lib:SOT-23-3, B.Cu at (152.0, 4.40)
- added TMR9: TMR2617, tmr-lib:SOT-23-3, B.Cu at (171.0, 4.40)
- added U4: ADG706BRU, Package_SO:TSSOP-28_4.4x9.7mm_P0.65mm, B.Cu at (118.6, 44.0)
- added U5: ADG706BRU, Package_SO:TSSOP-28_4.4x9.7mm_P0.65mm, B.Cu at (49.2, 59.9)
- added U6: ADG706BRU, Package_SO:TSSOP-28_4.4x9.7mm_P0.65mm, B.Cu at (146.2, 62.6)
- added U7: TPS22902, tmr-lib:Texas_DSBGA-4_0.8x0.8mm_Layout2x2_P0.4mm, B.Cu at (15.2, 56.8)
- C1: value 100nF -> 2.2uF; footprint tmr-lib:C_0603_1608Metric -> Capacitor_SMD:C_0603_1608Metric
- C10: value 2.2uF -> 0.1uF; footprint tmr-lib:C_0603_1608Metric -> Capacitor_SMD:C_0402_1005Metric
- C11: value 1uF -> 10uF; footprint tmr-lib:C_0603_1608Metric -> Capacitor_SMD:C_0603_1608Metric
- C2, C4, C5: value 100nF -> 10uF; footprint tmr-lib:C_0603_1608Metric -> Capacitor_SMD:C_0603_1608Metric
- C3: value 100nF -> 1uF; footprint tmr-lib:C_0603_1608Metric -> Capacitor_SMD:C_0603_1608Metric
- C6, C7, C8, C9: value 100nF -> 0.1uF; footprint tmr-lib:C_0603_1608Metric -> Capacitor_SMD:C_0402_1005Metric
- D1, D10, D11, D12, D13, D14, D15, D16, D17, D18, D19, D2, D20, D21, D22, D23, D24, D25, D26, D27, D28, D29, D3, D30, D31, D32, D33, D34, D35, D36, D37, D38, D39, D4, D40, D41, D42, D43, D44, D45, D46, D47, D48, D49, D5, D50, D51, D52, D53, D54, D55, D56, D57, D58, D59, D6, D60, D61, D62, D63, D64, D65, D66, D67, D68, D69, D7, D70, D71, D72, D8, D9: footprint tmr-lib:LED-6028 -> tmr-lib:LED_1206_3216Metric_ReverseMount_Hole2.1mm; moved to B.Cu
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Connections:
- net /GPIO4 renamed /SHPACT
- net /GPIO6 renamed /CHG
- C1 pad 1: +1V1 -> Net-(U1-VBUS)
- C10 pad 1: GND -> +2V1_TMR
- C10 pad 2: VBUS -> GND
- C11 pad 1: +1V1 -> GND
- C11 pad 2: GND -> +2V1
- C2 pad 1: +1V1 -> /VSYS
- C3 pad 1: +3V3 -> /VBAT
- C4 pad 1: +3V3 -> Net-(U1-DEC)
- C5 pad 1: +3V3 -> +2V1
- C6 pad 1: +3V3 -> +2V1_TMR
- C7 pad 1: +3V3 -> +2V1_TMR
- C8 pad 1: +3V3 -> +2V1_TMR
- C9 pad 1: +3V3 -> +2V1_TMR
- D1 pad 1: CA1 -> LED_CATH
- D1 pad 2: CA2 -> Net-(D1-A)
- D10 pad 1: CB1 -> LED_CATH
- D10 pad 2: CB3 -> Net-(D10-A)
- D11 pad 1: CB1 -> LED_CATH
- D11 pad 2: CB4 -> Net-(D11-A)
- D12 pad 1: CB1 -> LED_CATH
- D12 pad 2: CB5 -> Net-(D12-A)
- D13 pad 1: CB1 -> LED_CATH
- D13 pad 2: CB6 -> Net-(D13-A)
- D14 pad 1: CB1 -> LED_CATH
- D14 pad 2: CB7 -> Net-(D14-A)
- D15 pad 1: CB1 -> LED_CATH
- D15 pad 2: CB8 -> Net-(D15-A)
- D16 pad 1: CA2 -> LED_CATH
- D16 pad 2: CA1 -> Net-(D16-A)
- D17 pad 1: CA2 -> LED_CATH
- D17 pad 2: CA3 -> Net-(D17-A)
- D18 pad 1: CA2 -> LED_CATH
- D18 pad 2: CA4 -> Net-(D18-A)
- D19 pad 1: CA2 -> LED_CATH
- D19 pad 2: CA5 -> Net-(D19-A)
- D2 pad 1: CA1 -> LED_CATH
- D2 pad 2: CA3 -> Net-(D2-A)
- D20 pad 1: CA2 -> LED_CATH
- D20 pad 2: CA6 -> Net-(D20-A)
- D21 pad 1: CA2 -> LED_CATH
- D21 pad 2: CA7 -> Net-(D21-A)
- D22 pad 1: CA2 -> LED_CATH
- D22 pad 2: CA8 -> Net-(D22-A)
- D23 pad 1: CA2 -> LED_CATH
- D23 pad 2: CA9 -> Net-(D23-A)
- D24 pad 1: CB2 -> LED_CATH
- D24 pad 2: CB1 -> Net-(D24-A)
- D25 pad 1: CB2 -> LED_CATH
- D25 pad 2: CB3 -> Net-(D25-A)
- D26 pad 1: CB2 -> LED_CATH
- D26 pad 2: CB4 -> Net-(D26-A)
- D27 pad 1: CB2 -> LED_CATH
- D27 pad 2: CB5 -> Net-(D27-A)
- D28 pad 1: CB2 -> LED_CATH
- D28 pad 2: CB6 -> Net-(D28-A)
- D29 pad 1: CB2 -> LED_CATH
- D29 pad 2: CB7 -> Net-(D29-A)
- D3 pad 1: CA1 -> LED_CATH
- D3 pad 2: CA4 -> Net-(D3-A)
- D30 pad 1: CA3 -> LED_CATH
- D30 pad 2: CA1 -> Net-(D30-A)
- D31 pad 1: CA3 -> LED_CATH
- D31 pad 2: CA2 -> Net-(D31-A)
- D32 pad 1: CA3 -> LED_CATH
- D32 pad 2: CA4 -> Net-(D32-A)
- D33 pad 1: CA3 -> LED_CATH
- D33 pad 2: CA5 -> Net-(D33-A)
- D34 pad 1: CA3 -> LED_CATH
- D34 pad 2: CA6 -> Net-(D34-A)
- D35 pad 1: CA3 -> LED_CATH
- D35 pad 2: CA7 -> Net-(D35-A)
- D36 pad 1: CA3 -> LED_CATH
- D36 pad 2: CA8 -> Net-(D36-A)
- D37 pad 1: CA3 -> LED_CATH
- D37 pad 2: CA9 -> Net-(D37-A)
- D38 pad 1: CB3 -> LED_CATH
- D38 pad 2: CB1 -> Net-(D38-A)
- D39 pad 1: CB3 -> LED_CATH
- D39 pad 2: CB2 -> Net-(D39-A)
- D4 pad 1: CA1 -> LED_CATH
- D4 pad 2: CA5 -> Net-(D4-A)
- D40 pad 1: CB3 -> LED_CATH
- D40 pad 2: CB4 -> Net-(D40-A)
- D41 pad 1: CB3 -> LED_CATH
- D41 pad 2: CB5 -> Net-(D41-A)
- D42 pad 1: CB3 -> LED_CATH
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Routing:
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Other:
- board text removed: "${REFERENCE}"
